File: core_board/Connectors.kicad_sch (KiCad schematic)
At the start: 41 parts, among them J10 Conn_01x04_Pin, J11 Conn_01x02_Pin, J12 Conn_01x02_Pin, J13 Conn_01x04_Pin, J14 Conn_01x02_Pin, J15 Conn_01x02_Pin, J3 Conn_01x02_Pin, J4 Conn_01x04_Pin, J5 Conn_01x04_Pin, J6 Conn_01x02_Pin, J7 Conn_01x04_Pin, J8 Conn_01x04_Pin, J9 Conn_01x02_Pin, Q11 BSS138, Q13 BSS138, Q14 BSS138, Q16 BSS138, Q17 BSS138, Q18 BSS138, Q19 BSS138, Q20 BSS138, Q21 BSS138, Q9 BSS138

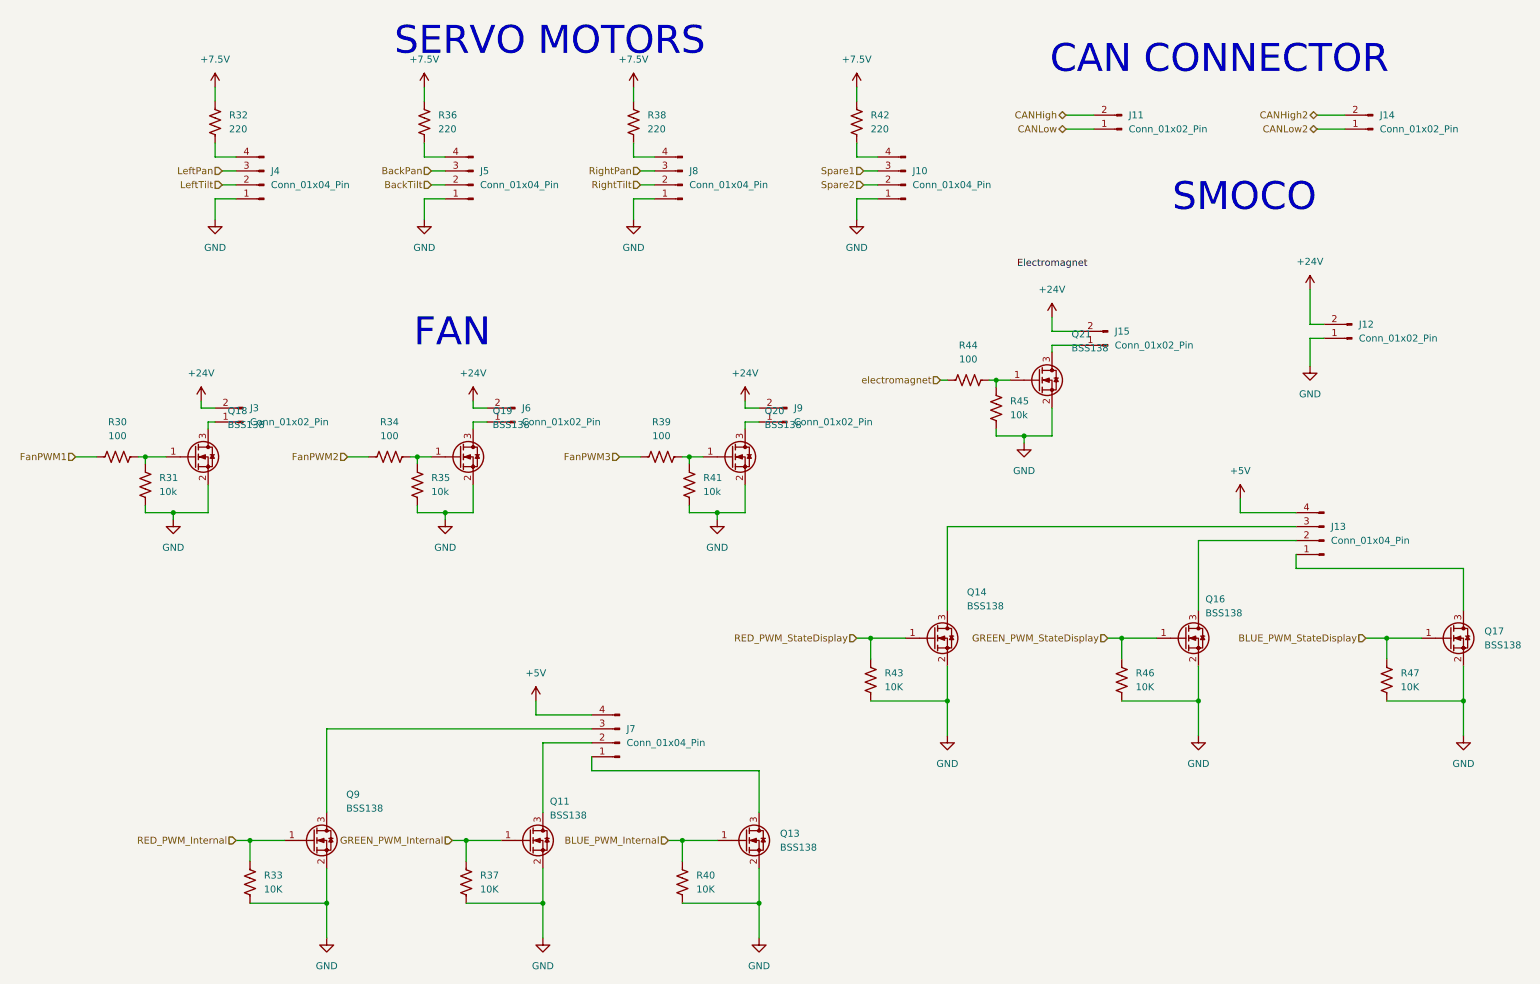
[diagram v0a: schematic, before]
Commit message: Add extra components
fixed LED connector
removed extra buck
fixed wrong footprints
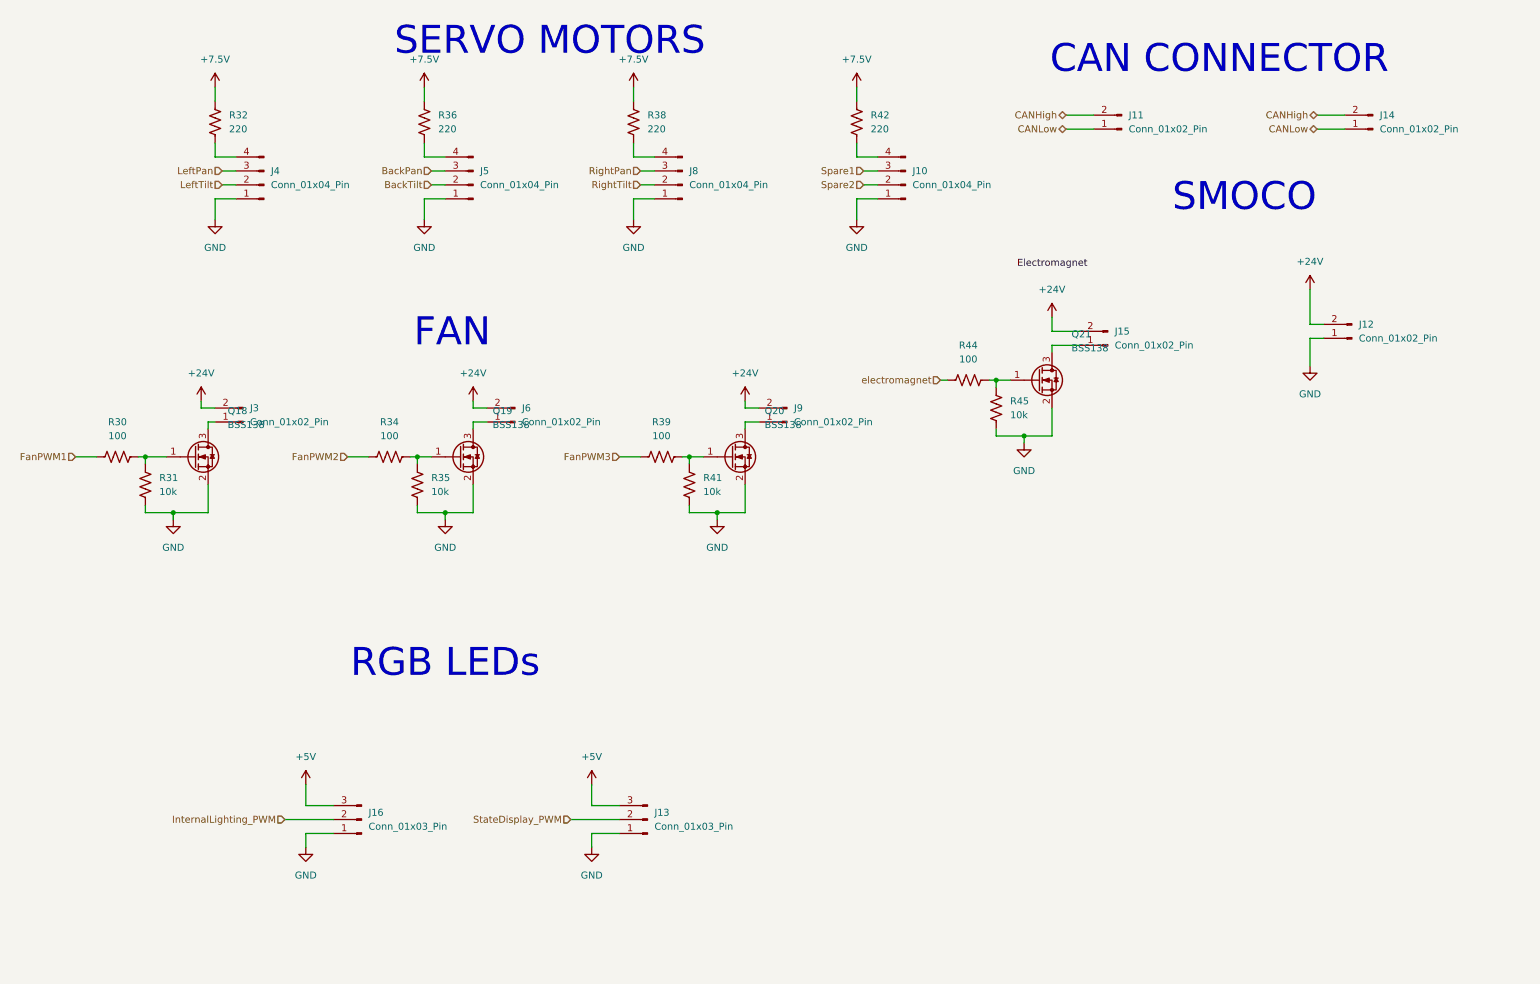
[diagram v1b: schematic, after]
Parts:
- removed J13, J7: Conn_01x04_Pin, Connector_JST:JST_PH_B4B-PH-K_1x04_P2.00mm_Vertical, symbol Connector:Conn_01x04_Pin
- removed Q11, Q13, Q14, Q16, Q17, Q9: BSS138, Package_TO_SOT_SMD:SOT-23, symbol Transistor_FET:BSS138
- removed R33, R37, R40, R43, R46, R47: 10K, Resistor_SMD:R_0603_1608Metric_Pad0.98x0.95mm_HandSolder, symbol Device:R_US
- added J13, J16: Conn_01x03_Pin, Connector_JST:JST_PH_B3B-PH-K_1x03_P2.00mm_Vertical, symbol Connector:Conn_01x03_Pin
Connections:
- net CANHigh2 is gone; now on net CANHigh: J14.2 (Pin_2)
- net CANLow2 is gone; now on net CANLow: J14.1 (Pin_1)
- net +5V: now also J13.3 (Pin_3), J16.3 (Pin_3)
- net GND: now also J13.1 (Pin_1), J16.1 (Pin_1)
- new net InternalLighting_PWM: J16.2 (Pin_2)
- new net StateDisplay_PWM: J13.2 (Pin_2)
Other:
- note added: "RGB LEDs"

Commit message: layout Stuff
some changes to layout footprints
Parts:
- renumbered J4 to J4Serv1, R32 to R32Serv1
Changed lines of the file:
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@@
 		(dnp no)
 		(fields_autoplaced yes)
-		(property "Reference" "J4"
+		(property "Reference" "J4Serv1"
 			(at 58.42 49.5299 0)
 			(show_name no)
@@
 			(project "core_board"
 				(path "/e01d6047-065c-44c8-9643-8ab57e6ffae6/1e3ab302-e360-416c-88e3-133e033fb1f0"
-					(reference "J4")
+					(reference "J4Serv1")
 					(unit 1)
 				)
@@
 		(dnp no)
 		(fields_autoplaced yes)
-		(property "Reference" "R32"
+		(property "Reference" "R32Serv1"
 			(at 50.8 39.3699 0)
 			(show_name no)
@@
 			(project "core_board"
 				(path "/e01d6047-065c-44c8-9643-8ab57e6ffae6/1e3ab302-e360-416c-88e3-133e033fb1f0"
-					(reference "R32")
-					(unit 1)
-				)
+					(reference "R32Serv1")
+					(unit 1)
+				)

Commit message: Layout updates
footprint changes
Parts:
- J3: footprint Converter_DCDC:Converter_DCDC_Cyntec_MUN12AD01-SH -> Connector_JST:JST_PH_B2B-PH-K_1x02_P2.00mm_Vertical
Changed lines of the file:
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@@
 			)
 		)
-		(property "Footprint" "Converter_DCDC:Converter_DCDC_Cyntec_MUN12AD01-SH"
+		(property "Footprint" "Connector_JST:JST_PH_B2B-PH-K_1x02_P2.00mm_Vertical"
 			(at 53.34 95.25 0)
 			(hide yes)

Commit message: Fix Smoco power connector
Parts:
- J12: footprint Connector_JST:JST_PH_B2B-PH-K_1x02_P2.00mm_Vertical -> MRDT_Connectors:MOLEX_MegaFit_02_Vertical
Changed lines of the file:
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@@
 			)
 		)
-		(property "Footprint" "Connector_JST:JST_PH_B2B-PH-K_1x02_P2.00mm_Vertical"
+		(property "Footprint" "MRDT_Connectors:MOLEX_MegaFit_02_Vertical"
 			(at 255.27 80.01 0)
 			(hide yes)
